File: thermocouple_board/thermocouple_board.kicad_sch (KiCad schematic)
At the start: 14 parts, among them J1 Screw_Terminal, J16 Conn_02x18_Odd_Even, J7 DSUB1, U1 MAX31856, U10 TCA9548A_Breakout, U11 PCF8575_Breakout

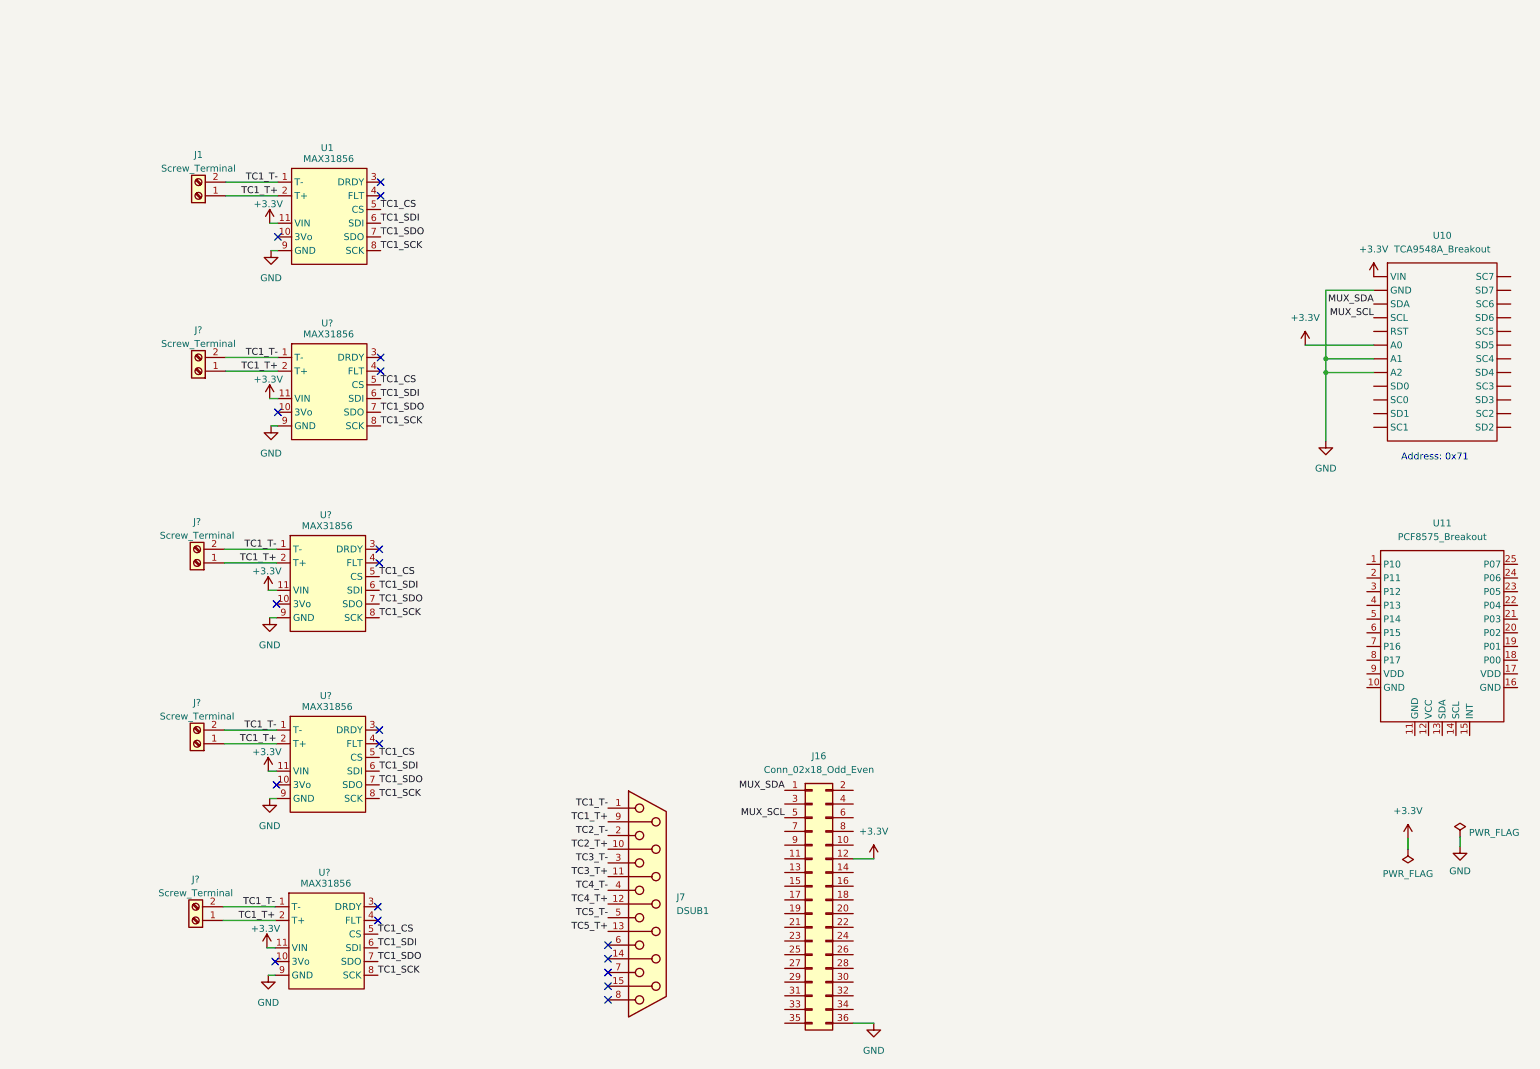
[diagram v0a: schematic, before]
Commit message: Finished thermocouple board.
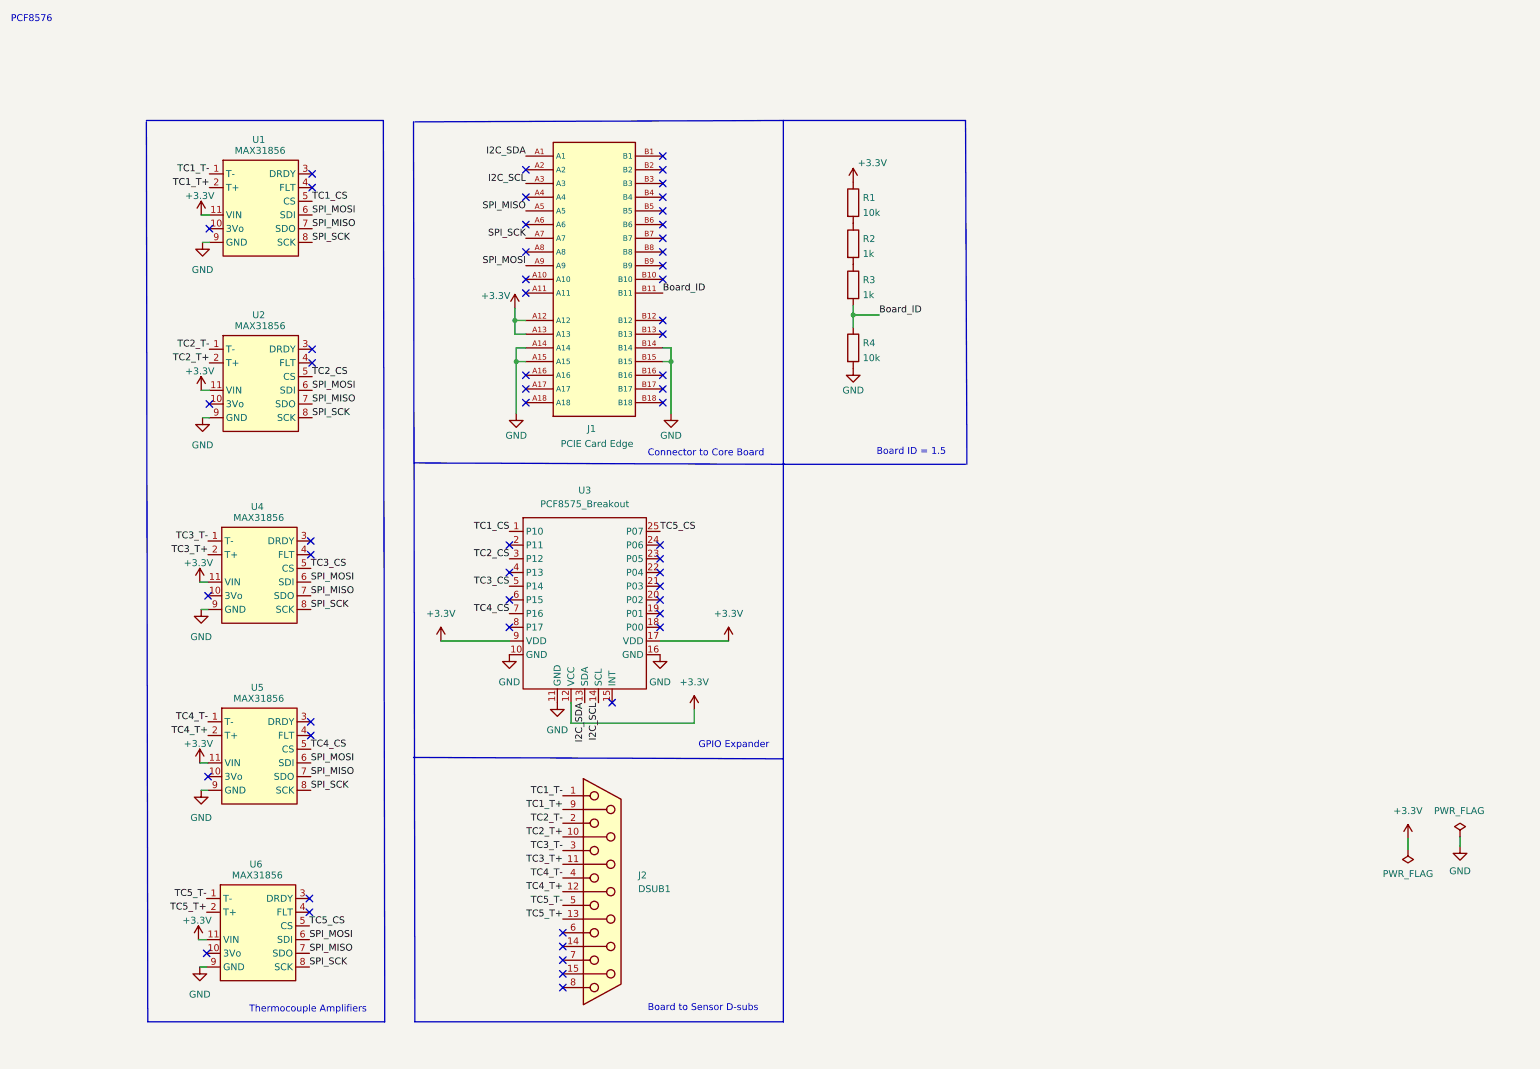
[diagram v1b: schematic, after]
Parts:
- removed J1, J? (x4): Screw_Terminal, symbol Connector:Screw_Terminal_01x02
- removed U10: TCA9548A_Breakout, symbol TCA9548A_Breakout:TCA9548A_Breakout
- added R1, R4: 10k, Resistor_SMD:R_0603_1608Metric, symbol Device:R
- added R2, R3: 1k, Resistor_SMD:R_0603_1608Metric, symbol Device:R
- J1: renamed from J16; value Conn_02x18_Odd_Even -> PCIE Card Edge; footprint (none) -> Connector_PCBEdge:BUS_PCIexpress_x1; symbol Connector_Generic:Conn_02x18_Odd_Even -> PCIE_Card_Edge:PCIE-LP-01-01-F-DV-A-TR_(card_edge)
- J2: renamed from J7; footprint (none) -> DSUB_622-015-260-042:DSUB_622-015-260-042
- U1: footprint (none) -> MAX31856_Breakout:MAX31856_Breakout
- U2, U4, U5, U6: renamed from U?; footprint (none) -> MAX31856_Breakout:MAX31856_Breakout
- U3: renamed from U11; footprint (none) -> PCF8575_Breakout:PCF8575_Breakout
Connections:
- net +3V3: now also J1.A12, J1.A13, U3.12 (VCC), U3.17 (VDD), U3.9 (VDD), R1.1; no longer J1.12 (Pin_12)
- net GND: now also J1.A14, J1.A15, J1.B14, J1.B15, U3.10 (GND), U3.11 (GND), U3.16 (GND), R4.2; no longer J1.36 (Pin_36)
- net TC1_CS: now also U3.1 (P10); no longer U2.5 (CS), U4.5 (CS), U5.5 (CS), U6.5 (CS)
- net TC1_T+: no longer U2.2 (T+), U4.2 (T+), U5.2 (T+), U6.2 (T+)
- net TC1_T-: no longer U2.1 (T-), U4.1 (T-), U5.1 (T-), U6.1 (T-)
- net TC2_T+: now also U2.2 (T+)
- net TC2_T-: now also U2.1 (T-)
- net TC3_T+: now also U4.2 (T+)
- net TC3_T-: now also U4.1 (T-)
- net TC4_T+: now also U5.2 (T+)
- net TC4_T-: now also U5.1 (T-)
- net TC5_T+: now also U6.2 (T+)
- net TC5_T-: now also U6.1 (T-)
- net I2C_SDA: now reaches U3.13 (SDA)
- net I2C_SDA: now also J1.A1
- net I2C_SCL: now reaches U3.14 (SCL)
- net I2C_SCL: now also J1.A3
- net TC5_CS: now reaches U3.25 (P07)
- net TC5_CS: now also U6.5 (CS)
- net TC2_CS: now reaches U3.3 (P12)
- net TC2_CS: now also U2.5 (CS)
- net TC3_CS: now reaches U3.5 (P14)
- net TC3_CS: now also U4.5 (CS)
- net TC4_CS: now reaches U3.7 (P16)
- net TC4_CS: now also U5.5 (CS)
- removed net MUX_SCL: J1.5 (Pin_5)
- removed net MUX_SDA: J1.1 (Pin_1)
- net TC1_SCK renamed SPI_SCK
- net SPI_SCK: now also J1.A7
- net TC1_SDI renamed SPI_MOSI
- net SPI_MOSI: now also J1.A9
- net TC1_SDO renamed SPI_MISO
- net SPI_MISO: now also J1.A5
- new net: R1.2, R2.1
- new net: R2.2, R3.1
- new net Board_ID: J1.B11, R3.2, R4.1
- no-connect marks 20 -> 56
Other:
- note added: "Board ID = 1.5"
- note added: "Board to Sensor D-subs"
- note added: "Connector to Core Board"
- note added: "GPIO Expander"
- note added: "PCF8576"
- note added: "Thermocouple Amplifiers"
- note removed: "Address: 0x71"
- moved on the sheet: J1, J2, U1, U2, U3, U4, U5, U6
